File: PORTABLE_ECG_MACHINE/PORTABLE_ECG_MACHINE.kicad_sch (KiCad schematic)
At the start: 85 parts, among them IC1 AD8232ACPZ, J1 UART, J2 AudioJack3, J3 Li-Ion 3.7 CONN, J4 USB_C_Receptacle_USB2.0, J5 Conn_01x06_Male, Q1 BSS138, Q2 BSS138, SW1 SW_SPDT, U2 CP2102-GM, U3 ATmega328PB-A, U4 TC1262-33, U5 TP4056, U6 SSD1306, Y1 16MHZ

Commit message: BOM-README update
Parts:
- C1, C15, C17, C24: JLC PCB PART NUMBER (none) -> C2204347; LCSC (none) -> C2204347; LCSC Part # (none) -> C2204347
- C10, C11, C12, C22: JLC PCB PART NUMBER (none) -> C2237744; LCSC (none) -> C2237744; LCSC Part # (none) -> C2237744
- C13: JLC PCB PART NUMBER (none) -> C2184695; LCSC (none) -> C2184695; LCSC Part # (none) -> C2184695
- C14: footprint Crystal:Crystal_SMD_2012-2Pin_2.0x1.2mm -> Capacitor_SMD:C_0603_1608Metric; JLC PCB PART NUMBER (none) -> C2184695; LCSC (none) -> C2184695; LCSC Part # (none) -> C2184695
- C16: JLC PCB PART NUMBER (none) -> C100040; LCSC (none) -> C100040; LCSC Part # (none) -> C100040
- C18: JLC PCB PART NUMBER (none) -> C107085; LCSC (none) -> C107085; LCSC Part # (none) -> C107085
- C19: JLC PCB PART NUMBER (none) -> C2185892; LCSC (none) -> C2185892; LCSC Part # (none) -> C2185892
- C2: value 100nf -> .1uf; JLC PCB PART NUMBER (none) -> C2237744; LCSC (none) -> C2237744; LCSC Part # (none) -> C2237744
- C20, C21, C3, C4, C5: JLC PCB PART NUMBER (none) -> C2168630; LCSC (none) -> C2168630; LCSC Part # (none) -> C2168630
- C23: JLC PCB PART NUMBER (none) -> C2167337; LCSC (none) -> C2167337; LCSC Part # (none) -> C2167337
- C6: value 2.2UF -> 2.2uf; JLC PCB PART NUMBER (none) -> C2858007; LCSC (none) -> C2858007; LCSC Part # (none) -> C2858007
- C7: value 10UF -> 10uf; JLC PCB PART NUMBER (none) -> C2167337; LCSC (none) -> C2167337; LCSC Part # (none) -> C2167337
- D1: JLC PCB PART NUMBER (none) -> C109002; LCSC (none) -> C109002; LCSC Part # (none) -> C109002
- D2, D3: JLC PCB PART NUMBER (none) -> C143772; LCSC (none) -> C143772; LCSC Part # (none) -> C143772
- DRIVE1, SELECT1: JLC PCB PART NUMBER (none) -> C221856; LCSC (none) -> C221856; LCSC Part # (none) -> C221856
- GREEN1: JLC PCB PART NUMBER (none) -> C2917809; LCSC (none) -> C2917809; LCSC Part # (none) -> C2917809
- IC1: JLC PCB PART NUMBER (none) -> C652575; LCSC (none) -> C652575; LCSC Part # (none) -> C652575
- J2: value AudioJack3 -> ECG PROBE; JLC PCB PART NUMBER (none) -> C2939151; LCSC (none) -> C2939151; LCSC Part # (none) -> C2939151
- J4: JLC PCB PART NUMBER (none) -> C2927026; LCSC (none) -> C2927026; LCSC Part # (none) -> C2927026
- Q1, Q2: JLC PCB PART NUMBER (none) -> C549757; LCSC (none) -> C549757; LCSC Part # (none) -> C549757
- R1: JLC PCB PART NUMBER (none) -> C2907166; LCSC (none) -> C2907166; LCSC Part # (none) -> C2907166
- R10, R12, R13, R14, R15, R16, R17, R18, R8, R9: JLC PCB PART NUMBER (none) -> C2907090; LCSC (none) -> C2907090; LCSC Part # (none) -> C2907090
- R11, R7: value 10K -> 10k; JLC PCB PART NUMBER (none) -> C2930027; LCSC (none) -> C2930027; LCSC Part # (none) -> C2930027
- R19: JLC PCB PART NUMBER (none) -> C2907115; LCSC (none) -> C2907115; LCSC Part # (none) -> C2907115
- R2, R3, R5, R6: JLC PCB PART NUMBER (none) -> C2930027; LCSC (none) -> C2930027; LCSC Part # (none) -> C2930027
- R20: value 330K -> 330k; JLC PCB PART NUMBER (none) -> C2907151; LCSC (none) -> C2907151; LCSC Part # (none) -> C2907151
- R21: value 100K -> 100k; JLC PCB PART NUMBER (none) -> C328419; LCSC (none) -> C328419; LCSC Part # (none) -> C328419
- R22: JLC PCB PART NUMBER (none) -> C2907088; LCSC (none) -> C2907088; LCSC Part # (none) -> C2907088
- R23, R24: JLC PCB PART NUMBER (none) -> C2913953; LCSC (none) -> C2913953; LCSC Part # (none) -> C2913953
- R4: value 390K -> 390k; JLC PCB PART NUMBER (none) -> C304747; LCSC (none) -> C304747; LCSC Part # (none) -> C304747
- RED1: JLC PCB PART NUMBER (none) -> C2917808; LCSC (none) -> C2917808; LCSC Part # (none) -> C2917808
- SW1: JLC PCB PART NUMBER (none) -> C2890358; LCSC (none) -> C2890358; LCSC Part # (none) -> C2890358
- U2: JLC PCB PART NUMBER (none) -> C6568; LCSC (none) -> C6568; LCSC Part # (none) -> C6568
- U3: JLC PCB PART NUMBER (none) -> C194192; LCSC (none) -> C194192; LCSC Part # (none) -> C194192
- U4: value TC1262-33 -> LM3940IMP-3.3/NOPB; JLC PCB PART NUMBER (none) -> C140319; LCSC (none) -> C140319; LCSC Part # (none) -> C140319; MANUFACTURER (none) -> (none)
- U5: JLC PCB PART NUMBER (none) -> C725790; LCSC (none) -> C725790; LCSC Part # (none) -> C725790; MANUFACTURER NanJing Top Power ASIC Corp. -> UMW(Youtai Semiconductor Co., Ltd.)
- U6: JLC PCB PART NUMBER (none) -> C2890600; LCSC (none) -> C2890600; LCSC Part # (none) -> C2890600
- Y1: JLC PCB PART NUMBER (none) -> C112972; LCSC (none) -> C112972; LCSC Part # (none) -> C112972

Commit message: REV 3
footprint change tp4056,add new 3d model oled 128*64,kicad render imgs add
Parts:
- U5: footprint Package_TO_SOT_SMD:TSOT-23-8 -> tp4056 ftprnt:SOP127P600X175-9N
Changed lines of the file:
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@@
     (property "Reference" "U5" (id 0) (at 112.522 231.013 0))
     (property "Value" "TP4056" (id 1) (at 112.522 233.553 0))
-    (property "Footprint" "Package_TO_SOT_SMD:TSOT-23-8" (id 2) (at 112.522 248.793 0)
+    (property "Footprint" "tp4056 ftprnt:SOP127P600X175-9N" (id 2) (at 112.522 248.793 0)
       (effects (font (size 1.27 1.27)) (justify left bottom) hide)
     )
@@
     )
     (path "/962f53be-4796-4882-97a5-e23946b557e2"
-      (reference "U5") (unit 1) (value "TP4056") (footprint "Package_TO_SOT_SMD:TSOT-23-8")
+      (reference "U5") (unit 1) (value "TP4056") (footprint "tp4056 ftprnt:SOP127P600X175-9N")
     )
     (path "/652955b7-3515-4c2d-9b6d-72d16d4413b9"

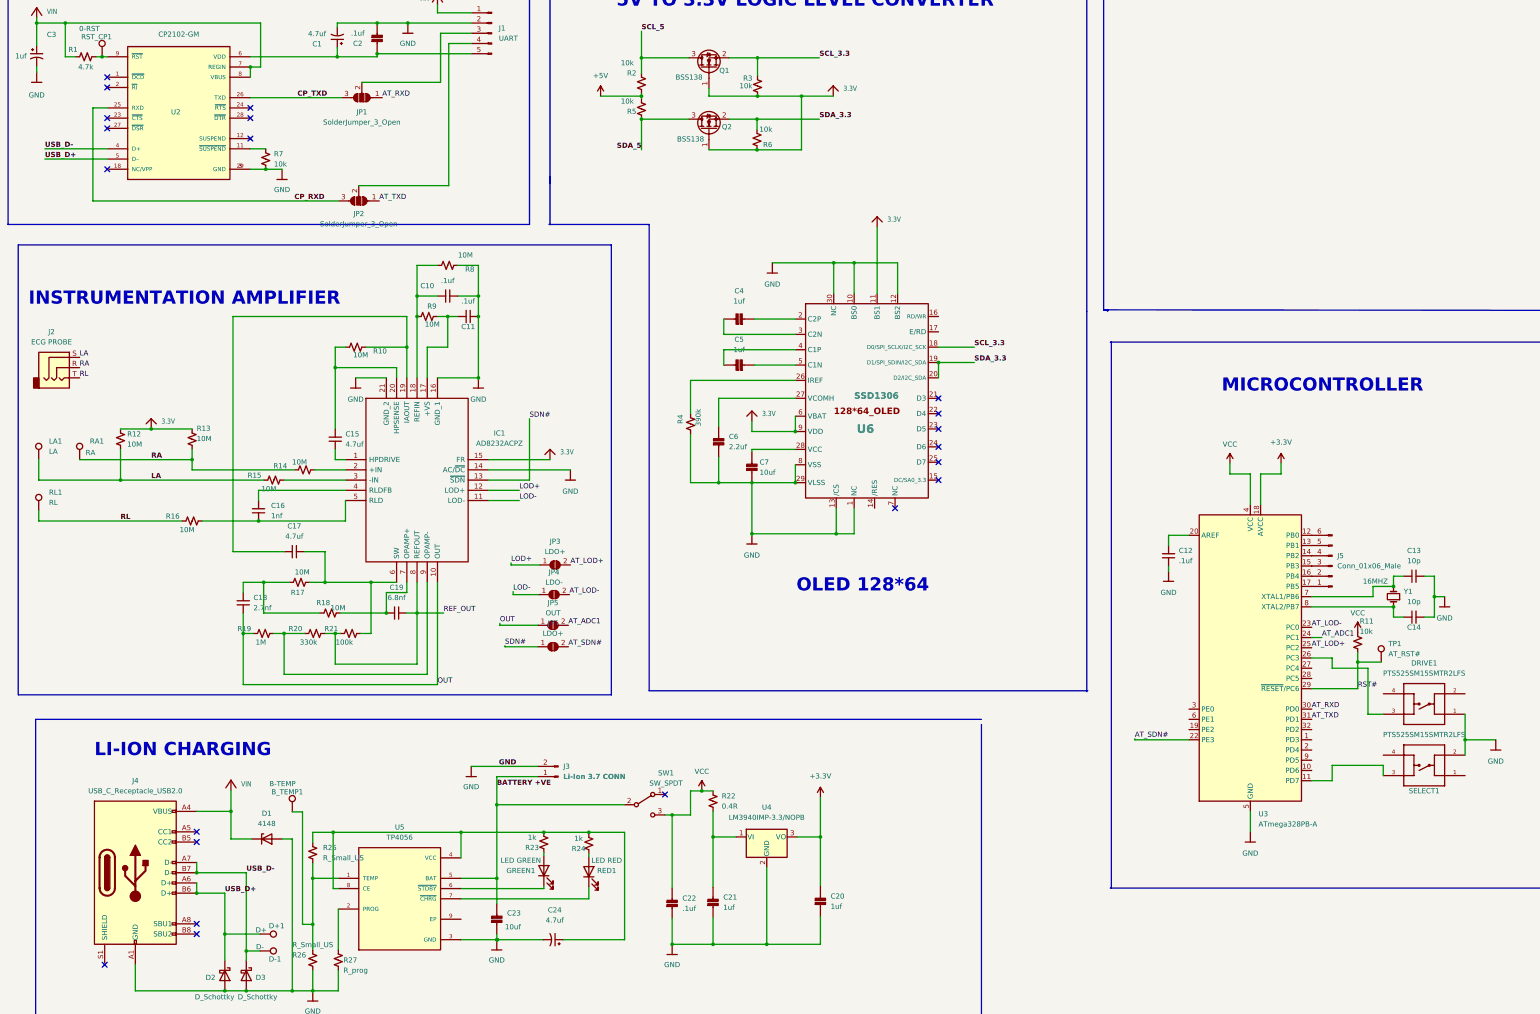
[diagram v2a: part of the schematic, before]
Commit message: schematics update
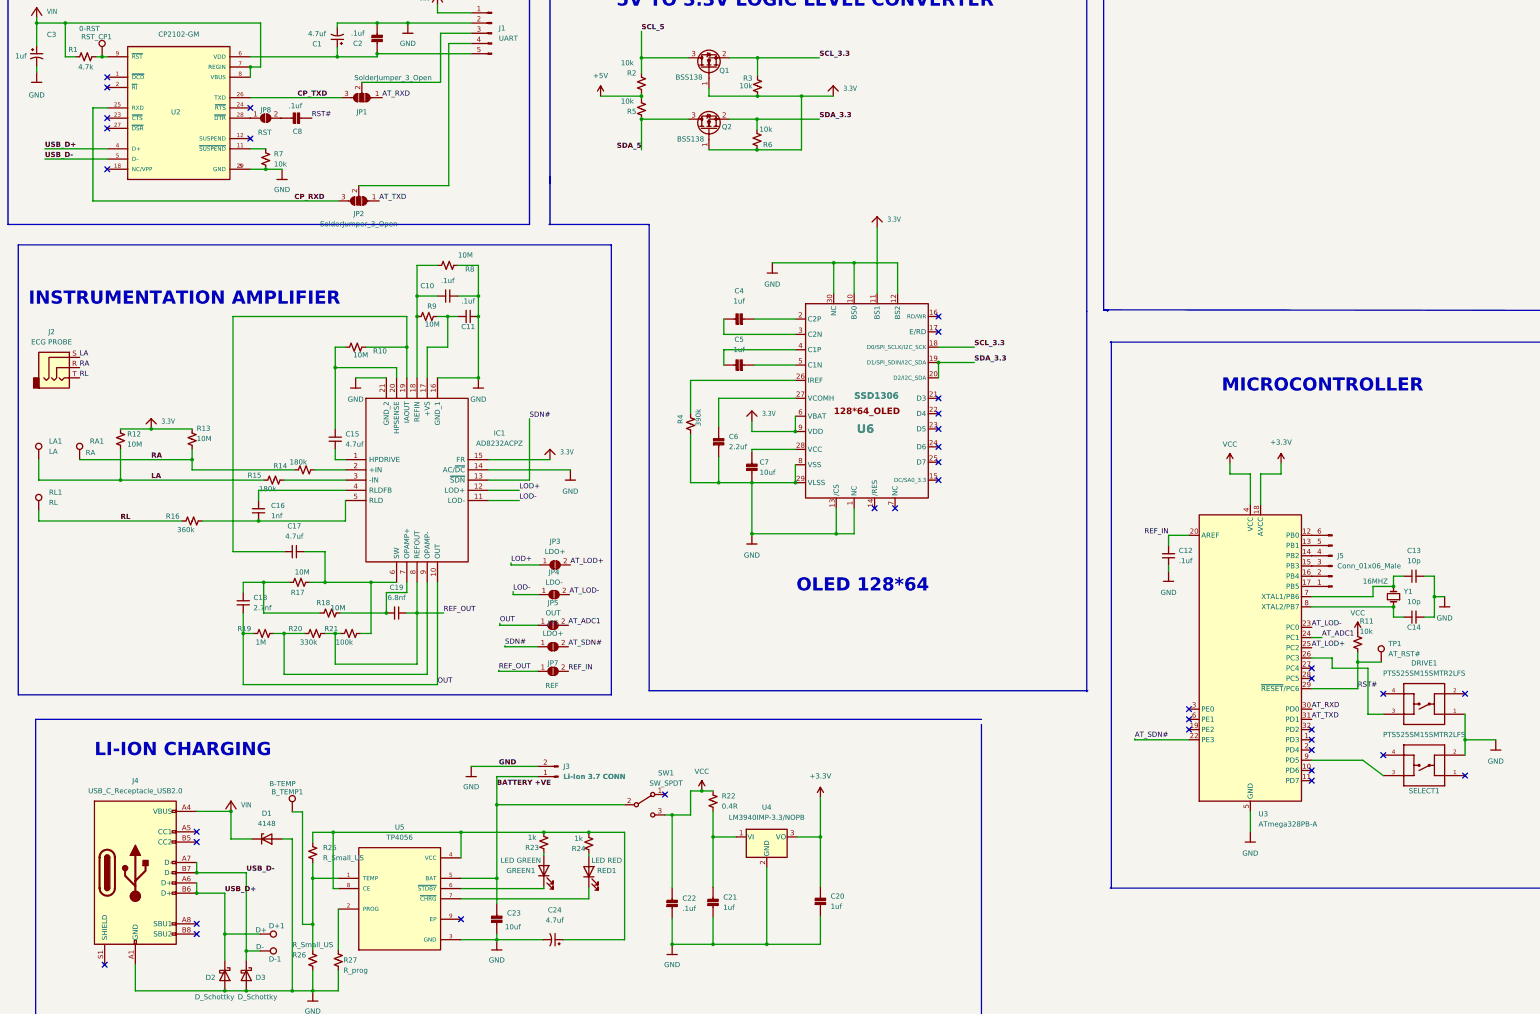
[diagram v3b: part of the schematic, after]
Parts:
- added C8: .1uf, Capacitor_SMD:C_0603_1608Metric, symbol Adafruit OLED 128x32 Mono I2C-eagle-import:CAP_CERAMIC0805-NOTHERMALS
- added JP7: REF, TEST_POINT_MATRIX_6-PIN:2_PIN_SMD_SOLDER_JUMPER, symbol Jumper:SolderJumper_2_Open
- added JP8: RST, TEST_POINT_MATRIX_6-PIN:2_PIN_SMD_SOLDER_JUMPER, symbol Jumper:SolderJumper_2_Open
- R14, R15: value 10M -> 180k
- R16: value 10M -> 360k
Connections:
- net GND: now also C24.2
- net REF_OUT: now also JP7.1 (A)
- net RST#: now also C8.2 (P$2)
- net USB_D+: now also U2.4 (D+); no longer U2.5 (D–)
- net USB_D-: now also U2.5 (D–); no longer U2.4 (D+)
- net REF_IN: now reaches C12.2, U3.20 (AREF)
- net REF_IN: now also JP7.2 (B)
- net at U3.11 (PD7): no longer SELECT1.3
- net at U3.9 (PD5): now also SELECT1.3
- net at U2.28 (~{DTR}): now also JP8.1 (A)
- new net: C8.1 (P$1), JP8.2 (B)
- no-connect marks 21 -> 38
